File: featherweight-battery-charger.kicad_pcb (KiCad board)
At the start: 2 copper layers, 20.3 x 32.7 mm, 13 parts, among them J2 Conn_01x02, J3 Conn_01x02, J4 Conn_01x02, U1 MCP73832-2-OT

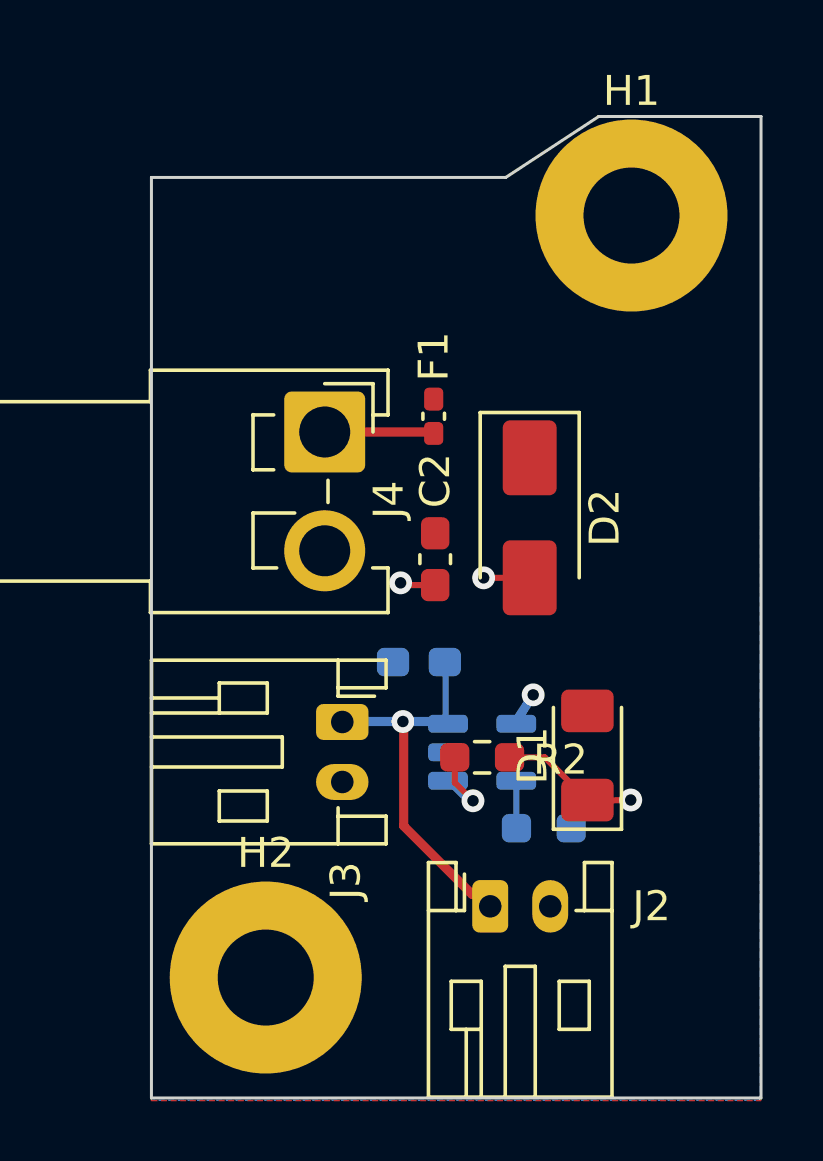
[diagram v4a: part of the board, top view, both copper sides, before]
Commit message: Fixed up Silkscreen
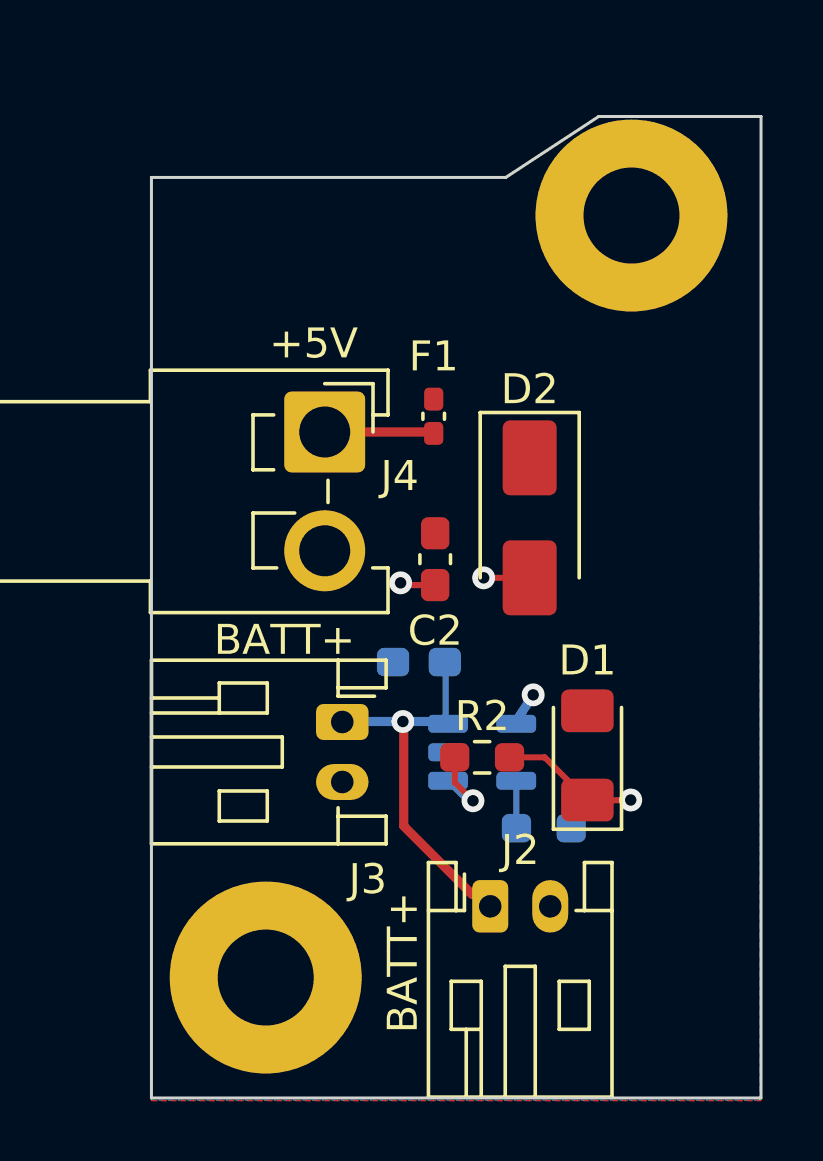
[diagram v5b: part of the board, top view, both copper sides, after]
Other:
- board text added: "+5V"
- board text added: "BATT+"
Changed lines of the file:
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@@
 		(tags "Diode SMA (DO-214AC)")
 		(property "Reference" "D2"
-			(at 0 -2.5 90)
+			(at -4.2848 0 180)
 			(layer "F.SilkS")
 			(effects
@@
 		(tags "fuse handsolder")
 		(property "Reference" "F1"
-			(at 1.9929 0 90)
+			(at 1.9929 0 180)
 			(layer "F.SilkS")
 			(effects
@@
 		(tags "connector JST VH horizontal")
 		(property "Reference" "J4"
-			(at 2.2582 -2.1336 90)
+			(at 1.472 -2.5 180)
 			(layer "F.SilkS")
 			(effects
@@
 		(tags "resistor handsolder")
 		(property "Reference" "R2"
-			(at -2.6111 -0.08 0)
+			(at 0 1.3716 180)
 			(layer "F.SilkS")
 			(effects
@@
 		(tags "connector JST PH horizontal")
 		(property "Reference" "J3"
-			(at 5.2926 -0.1154 270)
+			(at 5.2418 -0.852 0)
 			(layer "F.SilkS")
 			(effects
@@
 			(at 0 -4.15 0)
 			(layer "F.SilkS")
+			(hide yes)
 			(effects
 				(font
@@
 		(tags "connector JST PH horizontal")
 		(property "Reference" "J2"
-			(at 5.3782 0 0)
+			(at 1 -1.8746 180)
 			(layer "F.SilkS")
 			(effects
@@
 		(tags "LED handsolder")
 		(property "Reference" "D1"
-			(at 0 -1.83 90)
+			(at 3.1639 0 180)
 			(layer "F.SilkS")
 			(effects
@@
 		(tags "capacitor handsolder")
 		(property "Reference" "C2"
-			(at -2.6173 0 90)
+			(at 2.3877 0 180)
 			(layer "F.SilkS")
 			(effects
@@
 			(at 0 -4.15 0)
 			(layer "F.SilkS")
+			(hide yes)
 			(effects
 				(font
@@
 		(tags "SOT TO_SOT_SMD")
 		(property "Reference" "U1"
-			(at 0.036098 -2.5608 0)
+			(at 0.4064 -2.5248 0)
 			(layer "B.SilkS")
 			(effects
@@
 		(tags "resistor handsolder")
 		(property "Reference" "R1"
-			(at 2.7305 -0.041598 0)
+			(at 2.5908 0.0359 0)
 			(layer "B.SilkS")
 			(effects
@@
 		(layer "User.2")
 	)
+	(gr_text "+5V"
+		(at 147.6902 82.0674 0)
+		(layer "F.SilkS")
+		(effects
+			(font
+				(size 1 1)
+				(thickness 0.1)
+			)
+			(justify left bottom)
+		)
+	)
+	(gr_text "BATT+"
+		(at 152.7302 104.4702 90)
+		(layer "F.SilkS")
+		(effects
+			(font
+				(size 1 1)
+				(thickness 0.1)
+			)
+			(justify left bottom)
+		)
+	)
+	(gr_text "BATT+"
+		(at 145.8468 91.948 0)
+		(layer "F.SilkS")
+		(effects
+			(font
+				(size 1 1)
+				(thickness 0.1)
+			)
+			(justify left bottom)
+		)
+	)
 	(dimension

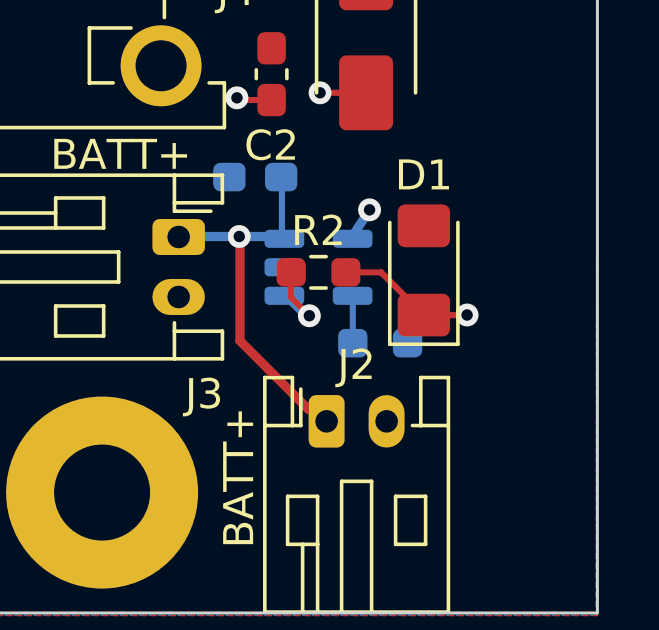
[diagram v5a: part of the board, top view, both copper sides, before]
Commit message: Remove seemingly pointless via
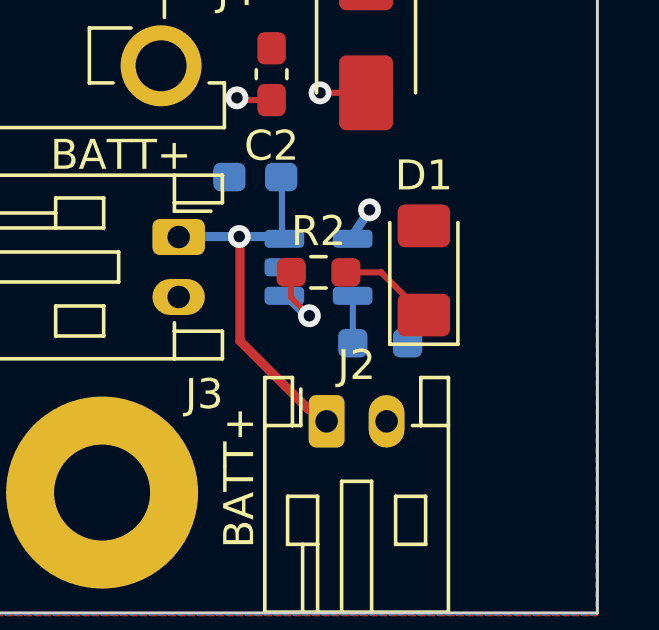
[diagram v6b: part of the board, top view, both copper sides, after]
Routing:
- net Net-(D1-K): track 4.64 -> 3.22 mm, vias 1 -> 0
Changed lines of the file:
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@@
-	)
-	(segment
-		(start 159.7406 96.6978)
-		(end 158.3211 96.7232)
-		(width 0.2032)
-		(layer "F.Cu")
-		(net 5)
 	)
 	(segment
@@
 		(net 5)
 	)
-	(via
-		(at 159.7406 96.6978)
-		(size 0.762)
-		(drill 0.381)
-		(layers "F.Cu" "B.Cu")
-		(net 5)
-	)

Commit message: Change C2 from 1uF to 4.7uF
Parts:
- C2: value 1uF -> 4.7uF
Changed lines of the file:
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@@
 			)
 		)
-		(property "Value" "1uF"
+		(property "Value" "4.7uF"
 			(at 0 1.43 90)
 			(layer "F.Fab")

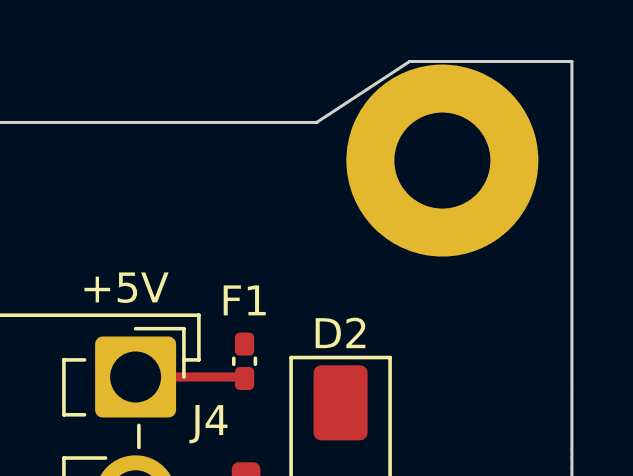
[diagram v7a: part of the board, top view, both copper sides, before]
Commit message: Fixed Dimensions to Line Holes up with Featherweight
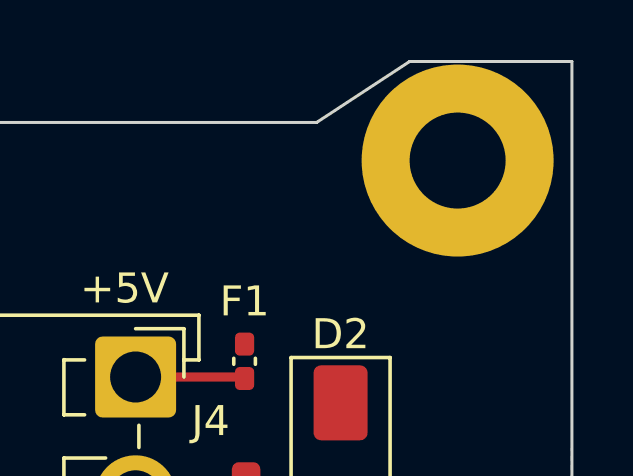
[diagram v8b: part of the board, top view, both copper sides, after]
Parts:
- moved H1 0.51 mm to (160.3, 77.2)
